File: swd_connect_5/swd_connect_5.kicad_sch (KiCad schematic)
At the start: 2 parts, among them J2 Link-E Receptacle, J3 swd-connect-5

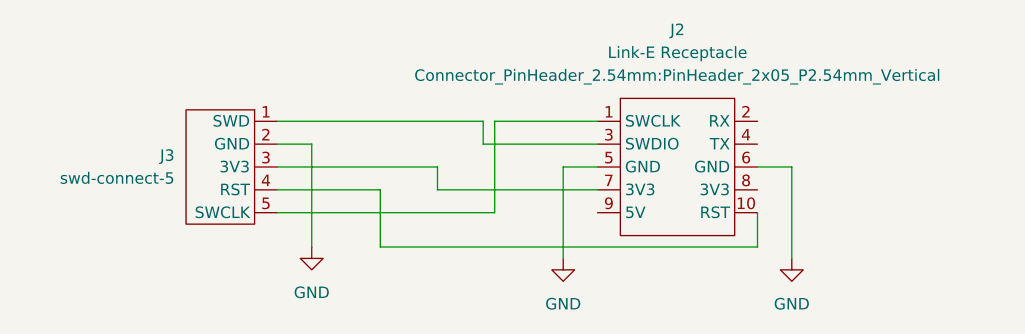
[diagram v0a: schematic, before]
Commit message: Update footprints to include silkscreen pin identifiers
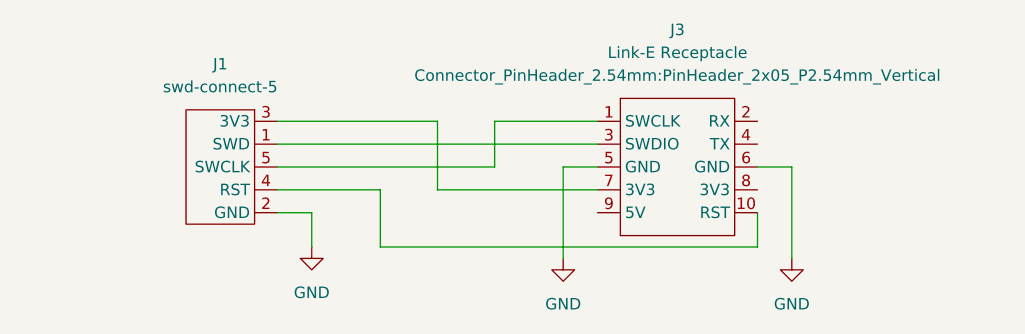
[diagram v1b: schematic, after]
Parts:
- removed J2: Link-E Receptacle, Connector_PinHeader_2.54mm:PinHeader_2x05_P2.54mm_Vertical, symbol zl4aa:Link-E
- removed J3: swd-connect-5, ZL4AA:swd-connect-5-programmer, symbol zl4aa:swd-connect-5
- added J1: swd-connect-5, swd-connect:swd-connect-5-programmer, symbol swd-connect:swd-connect-5
- added J3: Link-E Receptacle, Connector_PinHeader_2.54mm:PinHeader_2x05_P2.54mm_Vertical, symbol swd-connect:Link-E
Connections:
- net GND: now also J1.2 (GND), J3.5 (GND), J3.6 (GND)
- new net: J1.5 (SWCLK), J3.1 (SWCLK)
- new net: J1.4 (RST), J3.10 (RST)
- new net: J1.1 (SWD), J3.3 (SWDIO)
- new net: J1.3 (3V3), J3.7 (3V3)
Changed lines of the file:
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@@
+    (stroke (width 0) (type default))
+  )
+  (wire (pts (xy 121.92 101.6) (xy 121.92 97.79))
     (stroke (width 0) (type default))
   )
@@
     (stroke (width 0) (type default))
   )
-  (wire (pts (xy 140.97 87.63) (xy 140.97 90.17))
-    (stroke (width 0) (type default))
-  )
-  (wire (pts (xy 142.24 87.63) (xy 142.24 97.79))
-    (stroke (width 0) (type default))
-  )
-  (wire (pts (xy 140.97 90.17) (xy 153.67 90.17))
-    (stroke (width 0) (type default))
-  )
   (wire (pts (xy 149.86 92.71) (xy 149.86 102.87))
     (stroke (width 0) (type default))
   )
-  (wire (pts (xy 121.92 90.17) (xy 121.92 101.6))
+  (wire (pts (xy 142.24 87.63) (xy 142.24 92.71))
     (stroke (width 0) (type default))
   )
-  (wire (pts (xy 118.11 90.17) (xy 121.92 90.17))
+  (wire (pts (xy 135.89 95.25) (xy 135.89 87.63))
     (stroke (width 0) (type default))
   )
-  (wire (pts (xy 135.89 92.71) (xy 135.89 95.25))
+  (wire (pts (xy 121.92 97.79) (xy 118.11 97.79))
+    (stroke (width 0) (type default))
+  )
+  (wire (pts (xy 118.11 90.17) (xy 153.67 90.17))
     (stroke (width 0) (type default))
   )
@@
     (stroke (width 0) (type default))
   )
-  (wire (pts (xy 142.24 97.79) (xy 118.11 97.79))
+  (wire (pts (xy 135.89 87.63) (xy 118.11 87.63))
     (stroke (width 0) (type default))
   )
@@
     (stroke (width 0) (type default))
   )
-  (wire (pts (xy 118.11 87.63) (xy 140.97 87.63))
-    (stroke (width 0) (type default))
-  )
-  (wire (pts (xy 118.11 92.71) (xy 135.89 92.71))
+  (wire (pts (xy 118.11 92.71) (xy 142.24 92.71))
     (stroke (width 0) (type default))
   )
@@
     )
   )
-  (symbol (lib_id "zl4aa:Link-E") (at 162.56 92.71 0) (unit 1)
+  (symbol (lib_id "swd-connect:Link-E") (at 162.56 92.71 0) (unit 1)
     (in_bom yes) (on_board yes) (dnp no) (fields_autoplaced)
-    (property "Reference" "J2" (at 162.56 77.47 0)
+    (property "Reference" "J3" (at 162.56 77.47 0)
       (effects (font (size 1.27 1.27)))
     )
@@
       (project "swd_connect_5"
         (path "/213468be-7bdf-4b20-8406-766cdf385cd4"
-          (reference "J2") (unit 1)
+          (reference "J3") (unit 1)
         )
       )
-      (project "swd_connect"
-        (path "/318193d7-876b-4e23-b273-ef52b6ed065b"
+    )
+  )
+  (symbol (lib_id "swd-connect:swd-connect-5") (at 111.76 92.71 0) (mirror y) (unit 1)
+    (in_bom no) (on_board yes) (dnp no) (fields_autoplaced)
+    (property "Reference" "J1" (at 111.76 81.28 0)
+      (effects (font (size 1.27 1.27)))
+    )
+    (property "Value" "swd-connect-5" (at 111.76 83.82 0)
+      (effects (font (size 1.27 1.27)))
+    )
+    (property "Footprint" "swd-connect:swd-connect-5-programmer" (at 111.76 107.95 0)
+      (effects (font (size 1.27 1.27)) hide)
+    )
+    (property "Datasheet" "" (at 113.03 90.17 0)
+      (effects (font (size 1.27 1.27)) hide)
+    )
+    (pin "1")
+    (pin "2")
+    (pin "3")
+    (pin "4")
+    (pin "5")
+    (instances
+      (project "swd_connect_5"
+        (path "/213468be-7bdf-4b20-8406-766cdf385cd4"
           (reference "J1") (unit 1)
         )
@@
         )
       )
-    )
-  )
-  (symbol (lib_id "zl4aa:swd-connect-5") (at 111.76 92.71 0) (mirror y) (unit 1)
-    (in_bom no) (on_board yes) (dnp no)
-    (property "Reference" "J3" (at 106.68 91.44 0)
-      (effects (font (size 1.27 1.27)) (justify left))
-    )
-    (property "Value" "swd-connect-5" (at 106.68 93.98 0)
-      (effects (font (size 1.27 1.27)) (justify left))
-    )
-    (property "Footprint" "ZL4AA:swd-connect-5-programmer" (at 111.76 107.95 0)
-      (effects (font (size 1.27 1.27)) hide)
-    )
-    (property "Datasheet" "" (at 113.03 90.17 0)
-      (effects (font (size 1.27 1.27)) hide)
-    )
-    (pin "1")
-    (pin "2")
-    (pin "3")
-    (pin "4")
-    (pin "5")
-    (instances
-      (project "swd_connect_5"
-        (path "/213468be-7bdf-4b20-8406-766cdf385cd4"
-          (reference "J3") (unit 1)
-        )
-      )
